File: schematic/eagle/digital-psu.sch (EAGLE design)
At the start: 79 parts, among them IC1 TL072P, IC2 TLC272P, Q1 MPSA56-TO92, T3 2N3055, T4 2N3055, T5 2N3055, T6 2N3704, X1 Vout, X2 PASS_TRANSISTORS, X3 AC_IN

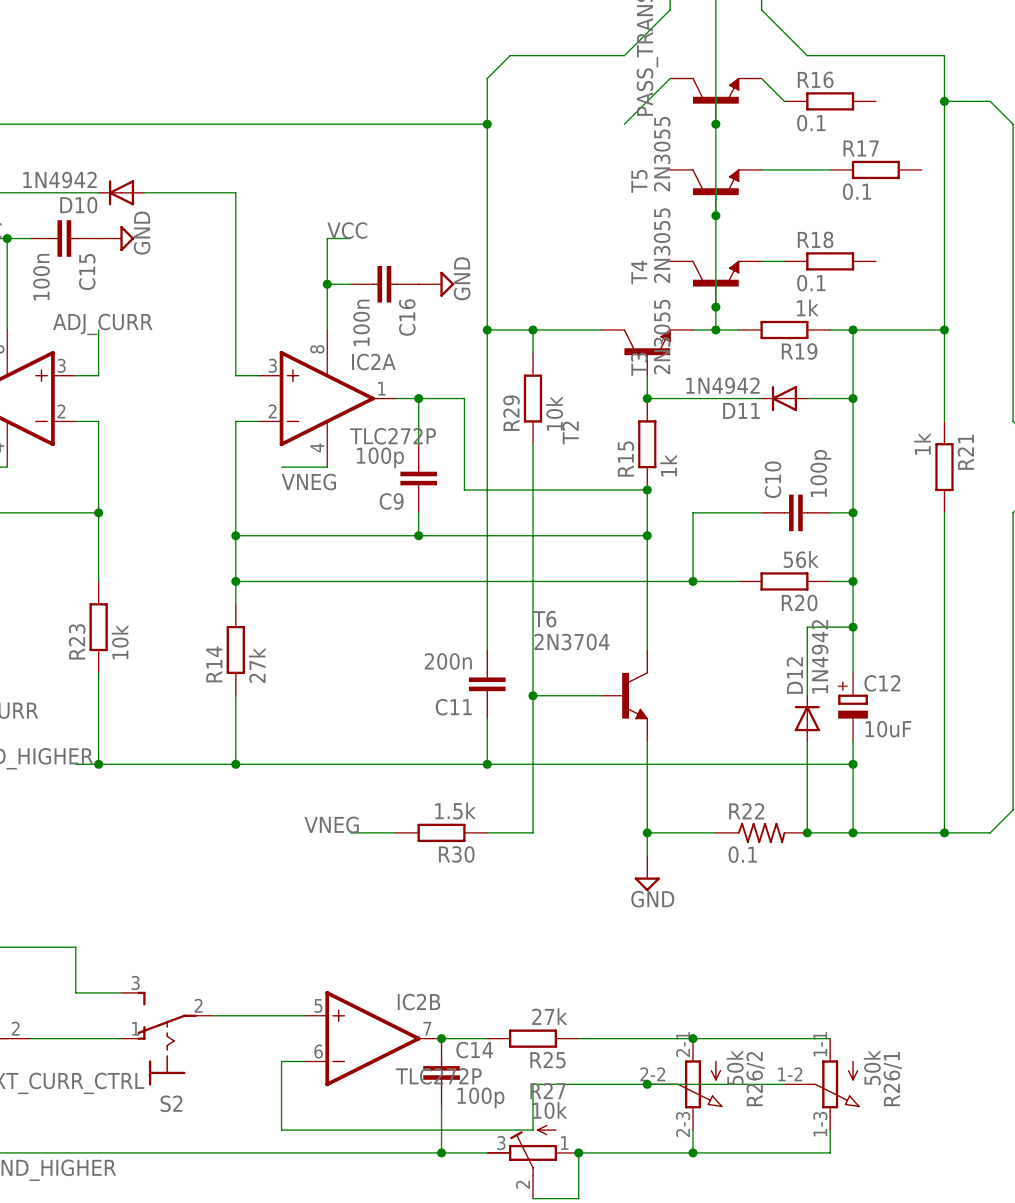
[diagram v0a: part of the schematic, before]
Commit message: routing board 85% from completion
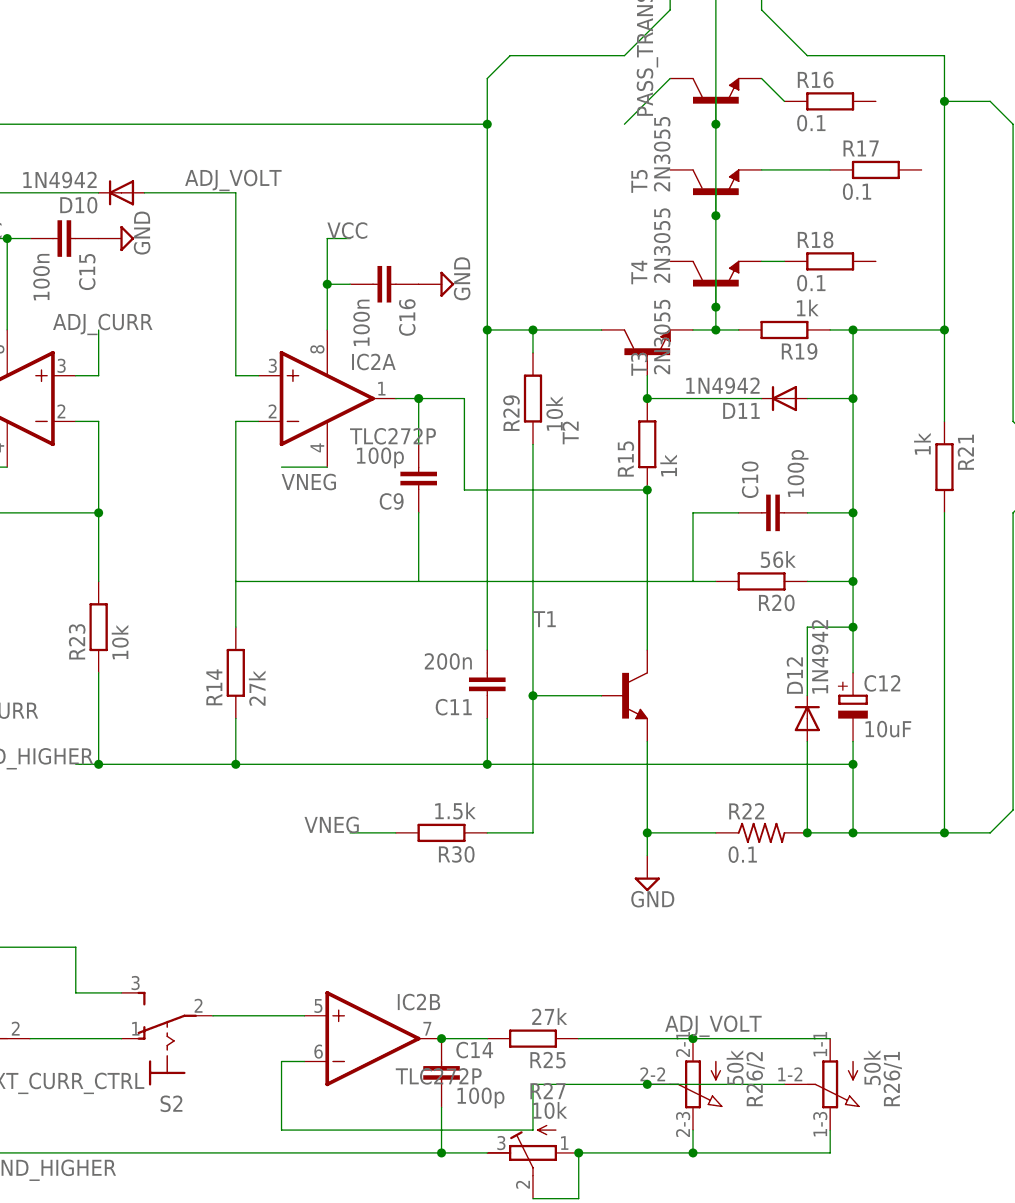
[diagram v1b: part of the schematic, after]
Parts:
- removed T6: 2N3704, transistor:2N3704
- added T1: (no value), transistor:-NPN-TO92-EBC
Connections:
- removed net N$10 (its old number): R29.1, R30.1, T6.B
- removed net N$18 (its old number): D10.A, IC2A.+IN
- removed net N$21: C10.1, C9.1, C9.2, IC2A.-IN, IC2A.OUT, R14.2, R15.1, R20.2, T6.C
- removed net N$22 (its old number): R25.1, R26/1.A, R26/2.A
- new net ADJ_VOLT: D10.A, IC2A.+IN, R25.1, R26/1.A, R26/2.A
- new net N$17: R29.1, R30.1, T1.B
- new net N$31: C9.2, IC2A.OUT, R15.1, T1.C
- new net N$38: C10.1, C9.1, IC2A.-IN, R14.2, R20.2
- net GND: now also T1.E; no longer T6.E
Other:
- moved on the sheet: C10, R14, R20
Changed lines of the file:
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@@
 <part name="R21" library="eagle-ltspice" deviceset="R" device="" value="1k"/>
 <part name="R22" library="rcl" deviceset="R-US_" device="VTA52" value="0.1"/>
-<part name="T6" library="transistor" deviceset="2N3704" device=""/>
 <part name="C11" library="rcl" deviceset="C-EU" device="C0805" value="200n"/>
 <part name="C12" library="resistor" deviceset="CPOL-EU" device="E5-10.5" value="10uF"/>
@@
 <part name="T7" library="transistor" deviceset="*-NPN-" device="TO92-EBC"/>
 <part name="VCC" library="con-wago-500" deviceset="W237-103" device="" value="VNEG"/>
+<part name="T1" library="transistor" deviceset="*-NPN-" device="TO92-EBC"/>
 </parts>
 <sheets>
@@
 <instance part="R12" gate="/2" x="213.36" y="248.92" rot="MR180"/>
 <instance part="D10" gate="1" x="241.3" y="307.34" rot="R180"/>
-<instance part="R14" gate="G$1" x="254" y="256.54" rot="R90"/>
+<instance part="R14" gate="G$1" x="254" y="254" rot="R90"/>
 <instance part="R15" gate="G$1" x="299.72" y="279.4" rot="R90"/>
 <instance part="C9" gate="G$1" x="274.32" y="274.32" rot="R180"/>
@@
 <instance part="IC2" gate="A" x="264.16" y="284.48"/>
 <instance part="IC2" gate="B" x="269.24" y="213.36"/>
-<instance part="R20" gate="G$1" x="314.96" y="264.16" rot="R180"/>
-<instance part="C10" gate="G$1" x="314.96" y="271.78" rot="R90"/>
+<instance part="R20" gate="G$1" x="312.42" y="264.16" rot="R180"/>
+<instance part="C10" gate="G$1" x="312.42" y="271.78" rot="R90"/>
 <instance part="R21" gate="G$1" x="332.74" y="276.86" rot="R270"/>
 <instance part="R22" gate="G$1" x="312.42" y="236.22"/>
-<instance part="T6" gate="G$1" x="297.18" y="251.46"/>
 <instance part="C11" gate="G$1" x="281.94" y="251.46" rot="R180"/>
 <instance part="C12" gate="G$1" x="322.58" y="251.46"/>
@@
 <instance part="VCC" gate="-2" x="60.96" y="220.98"/>
 <instance part="VCC" gate="-3" x="60.96" y="215.9"/>
+<instance part="T1" gate="G$1" x="297.18" y="251.46"/>
 </instances>
 <busses>
@@
 <pinref part="R22" gate="G$1" pin="1"/>
 <wire x1="307.34" y1="236.22" x2="299.72" y2="236.22" width="0.1524" layer="91"/>
-<pinref part="T6" gate="G$1" pin="E"/>
 <wire x1="299.72" y1="236.22" x2="299.72" y2="246.38" width="0.1524" layer="91"/>
 <wire x1="299.72" y1="236.22" x2="299.72" y2="233.68" width="0.1524" layer="91"/>
 <junction x="299.72" y="236.22"/>
 <pinref part="SUPPLY12" gate="GND" pin="GND"/>
+<pinref part="T1" gate="G$1" pin="E"/>
 </segment>
 <segment>
@@
 </segment>
 </net>
-<net name="N$17" class="0">
+<net name="N$18" class="0">
 <segment>
 <pinref part="C7" gate="G$1" pin="1"/>
@@
 </segment>
 </net>
-<net name="N$18" class="0">
-<segment>
-<wire x1="256.54" y1="287.02" x2="254" y2="287.02" width="0.1524" layer="91"/>
-<wire x1="254" y1="287.02" x2="254" y2="307.34" width="0.1524" layer="91"/>
-<wire x1="254" y1="307.34" x2="243.84" y2="307.34" width="0.1524" layer="91"/>
-<pinref part="D10" gate="1" pin="A"/>
-<pinref part="IC2" gate="A" pin="+IN"/>
-</segment>
-</net>
-<net name="N$21" class="0">
+<net name="N$31" class="0">
 <segment>
 <pinref part="C9" gate="G$1" pin="2"/>
@@
 <pinref part="R15" gate="G$1" pin="1"/>
 <wire x1="279.4" y1="274.32" x2="299.72" y2="274.32" width="0.1524" layer="91"/>
-<wire x1="299.72" y1="274.32" x2="299.72" y2="269.24" width="0.1524" layer="91"/>
 <junction x="299.72" y="274.32"/>
-<wire x1="299.72" y1="269.24" x2="274.32" y2="269.24" width="0.1524" layer="91"/>
-<pinref part="C9" gate="G$1" pin="1"/>
-<wire x1="274.32" y1="271.78" x2="274.32" y2="269.24" width="0.1524" layer="91"/>
 <pinref part="IC2" gate="A" pin="OUT"/>
-<pinref part="T6" gate="G$1" pin="C"/>
-<wire x1="299.72" y1="256.54" x2="299.72" y2="269.24" width="0.1524" layer="91"/>
-<junction x="299.72" y="269.24"/>
-<pinref part="R14" gate="G$1" pin="2"/>
-<wire x1="254" y1="261.62" x2="254" y2="264.16" width="0.1524" layer="91"/>
-<wire x1="254" y1="264.16" x2="254" y2="269.24" width="0.1524" layer="91"/>
-<wire x1="254" y1="269.24" x2="254" y2="281.94" width="0.1524" layer="91"/>
-<wire x1="254" y1="281.94" x2="256.54" y2="281.94" width="0.1524" layer="91"/>
-<pinref part="IC2" gate="A" pin="-IN"/>
-<pinref part="R20" gate="G$1" pin="2"/>
-<wire x1="309.88" y1="264.16" x2="304.8" y2="264.16" width="0.1524" layer="91"/>
-<junction x="254" y="264.16"/>
-<pinref part="C10" gate="G$1" pin="1"/>
-<wire x1="304.8" y1="264.16" x2="254" y2="264.16" width="0.1524" layer="91"/>
-<wire x1="312.42" y1="271.78" x2="304.8" y2="271.78" width="0.1524" layer="91"/>
-<wire x1="304.8" y1="271.78" x2="304.8" y2="264.16" width="0.1524" layer="91"/>
-<junction x="304.8" y="264.16"/>
-<wire x1="274.32" y1="269.24" x2="254" y2="269.24" width="0.1524" layer="91"/>
-<junction x="274.32" y="269.24"/>
-<junction x="254" y="269.24"/>
+<wire x1="299.72" y1="256.54" x2="299.72" y2="274.32" width="0.1524" layer="91"/>
+<pinref part="T1" gate="G$1" pin="C"/>
 </segment>
 </net>
@@
 </segment>
 </net>
-<net name="N$31" class="0">
+<net name="N$41" class="0">
 <segment>
 <pinref part="C10" gate="G$1" pin="2"/>
-<wire x1="320.04" y1="271.78" x2="322.58" y2="271.78" width="0.1524" layer="91"/>
+<wire x1="317.5" y1="271.78" x2="322.58" y2="271.78" width="0.1524" layer="91"/>
 <wire x1="322.58" y1="271.78" x2="322.58" y2="264.16" width="0.1524" layer="91"/>
 <pinref part="R20" gate="G$1" pin="1"/>
-<wire x1="322.58" y1="264.16" x2="320.04" y2="264.16" width="0.1524" layer="91"/>
+<wire x1="322.58" y1="264.16" x2="317.5" y2="264.16" width="0.1524" layer="91"/>
 <pinref part="D11" gate="1" pin="A"/>
 <wire x1="317.5" y1="284.48" x2="322.58" y2="284.48" width="0.1524" layer="91"/>
@@
 <junction x="238.76" y="243.84"/>
 <label x="223.52" y="243.84" size="1.778" layer="95"/>
-<wire x1="254" y1="243.84" x2="254" y2="251.46" width="0.1524" layer="91"/>
+<wire x1="254" y1="243.84" x2="254" y2="248.92" width="0.1524" layer="91"/>
 <junction x="254" y="243.84"/>
 <wire x1="322.58" y1="243.84" x2="322.58" y2="246.38" width="0.1524" layer="91"/>
@@
 </segment>
 </net>
-<net name="N$22" class="0">
+<net name="ADJ_VOLT" class="0">
 <segment>
 <pinref part="R25" gate="G$1" pin="1"/>
@@
 <wire x1="304.8" y1="213.36" x2="320.04" y2="213.36" width="0.1524" layer="91"/>
 <junction x="304.8" y="213.36"/>
+<label x="312.42" y="215.9" size="1.778" layer="95" rot="R180"/>
+</segment>
+<segment>
+<wire x1="256.54" y1="287.02" x2="254" y2="287.02" width="0.1524" layer="91"/>
+<wire x1="254" y1="287.02" x2="254" y2="307.34" width="0.1524" layer="91"/>
+<wire x1="254" y1="307.34" x2="243.84" y2="307.34" width="0.1524" layer="91"/>
+<pinref part="D10" gate="1" pin="A"/>
+<pinref part="IC2" gate="A" pin="+IN"/>
+<label x="259.08" y="309.88" size="1.778" layer="95" rot="R180"/>
 </segment>
 </net>
@@
 </segment>
 </net>
-<net name="N$33" class="0">
+<net name="N$22" class="0">
 <segment>
 <pinref part="S2" gate="1" pin="S"/>
@@
 </segment>
 </net>
-<net name="N$10" class="0">
+<net name="N$17" class="0">
 <segment>
 <pinref part="R29" gate="G$1" pin="1"/>
 <wire x1="287.02" y1="279.4" x2="287.02" y2="251.46" width="0.1524" layer="91"/>
-<pinref part="T6" gate="G$1" pin="B"/>
 <wire x1="287.02" y1="251.46" x2="294.64" y2="251.46" width="0.1524" layer="91"/>
 <wire x1="287.02" y1="251.46" x2="287.02" y2="236.22" width="0.1524" layer="91"/>
@@
 <pinref part="R30" gate="G$1" pin="1"/>
 <wire x1="287.02" y1="236.22" x2="281.94" y2="236.22" width="0.1524" layer="91"/>
-</segment>
-</net>
-<net name="N$37" class="0">
+<pinref part="T1" gate="G$1" pin="B"/>
+</segment>
+</net>
+<net name="N$10" class="0">
 <segment>
 <pinref part="R31" gate="G$1" pin="1"/>
@@
 </segment>
 </net>
+<net name="N$38" class="0">
+<segment>
+<pinref part="C9" gate="G$1" pin="1"/>
+<pinref part="IC2" gate="A" pin="-IN"/>
+<wire x1="254" y1="281.94" x2="256.54" y2="281.94" width="0.1524" layer="91"/>
+<pinref part="R14" gate="G$1" pin="2"/>
+<wire x1="254" y1="259.08" x2="254" y2="264.16" width="0.1524" layer="91"/>
+<pinref part="R20" gate="G$1" pin="2"/>
+<wire x1="254" y1="264.16" x2="254" y2="281.94" width="0.1524" layer="91"/>
+<wire x1="307.34" y1="264.16" x2="304.8" y2="264.16" width="0.1524" layer="91"/>
+<pinref part="C10" gate="G$1" pin="1"/>
+<wire x1="304.8" y1="264.16" x2="274.32" y2="264.16" width="0.1524" layer="91"/>
+<wire x1="274.32" y1="264.16" x2="254" y2="264.16" width="0.1524" layer="91"/>
+<wire x1="309.88" y1="271.78" x2="304.8" y2="271.78" width="0.1524" layer="91"/>
+<wire x1="304.8" y1="271.78" x2="304.8" y2="264.16" width="0.1524" layer="91"/>
+<wire x1="274.32" y1="271.78" x2="274.32" y2="264.16" width="0.1524" layer="91"/>
+</segment>
+</net>

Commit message: removed all airwires
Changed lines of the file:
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@@
 <pinref part="C10" gate="G$1" pin="1"/>
 <wire x1="304.8" y1="264.16" x2="274.32" y2="264.16" width="0.1524" layer="91"/>
-<wire x1="274.32" y1="264.16" x2="254" y2="264.16" width="0.1524" layer="91"/>
 <wire x1="309.88" y1="271.78" x2="304.8" y2="271.78" width="0.1524" layer="91"/>
-<wire x1="304.8" y1="271.78" x2="304.8" y2="264.16" width="0.1524" layer="91"/>
 <wire x1="274.32" y1="271.78" x2="274.32" y2="264.16" width="0.1524" layer="91"/>
+<wire x1="254" y1="264.16" x2="274.32" y2="264.16" width="0.1524" layer="91"/>
+<junction x="254" y="264.16"/>
+<junction x="274.32" y="264.16"/>
+<wire x1="304.8" y1="264.16" x2="304.8" y2="271.78" width="0.1524" layer="91"/>
+<junction x="304.8" y="264.16"/>
 </segment>
 </net>
